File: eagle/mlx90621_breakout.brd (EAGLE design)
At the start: 53.3 x 59.7 mm, 16 parts, among them J1 ARDUINO_R3_SHIELD

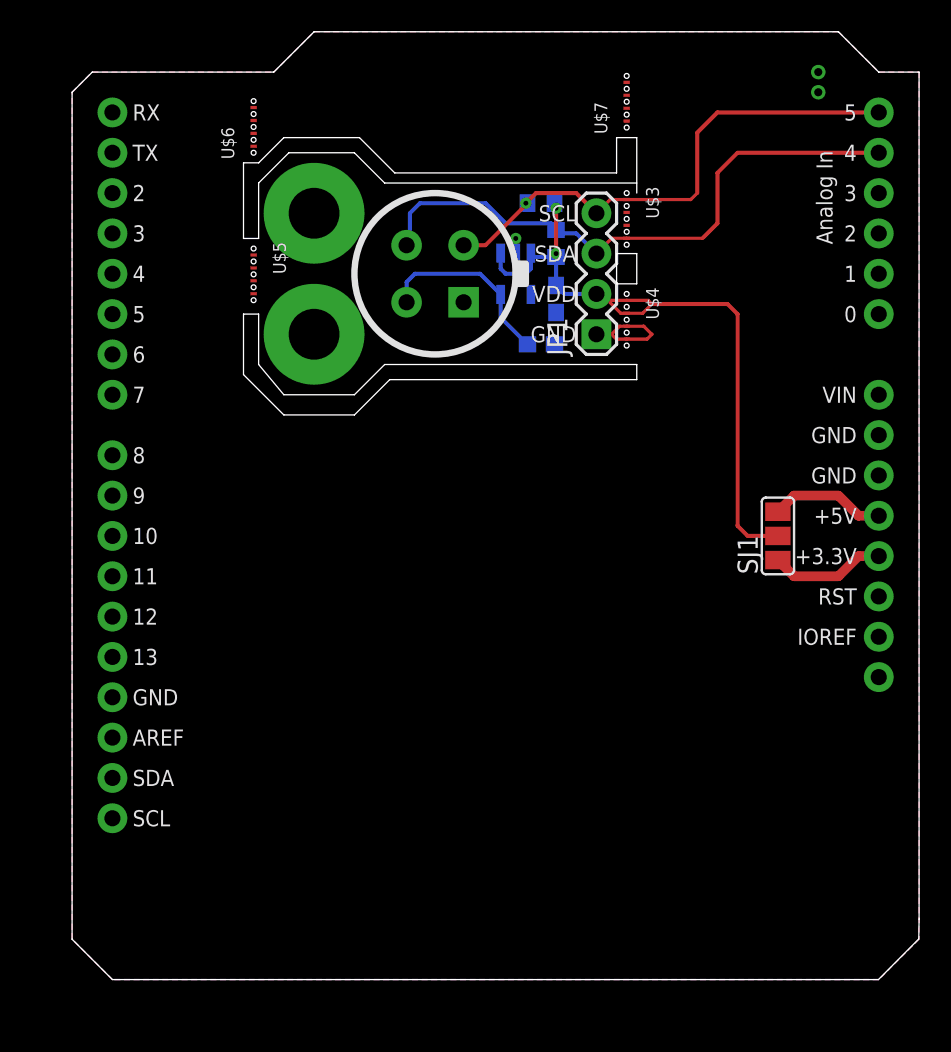
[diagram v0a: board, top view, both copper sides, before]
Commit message: cleaned breakout for better component counting at BOM generation
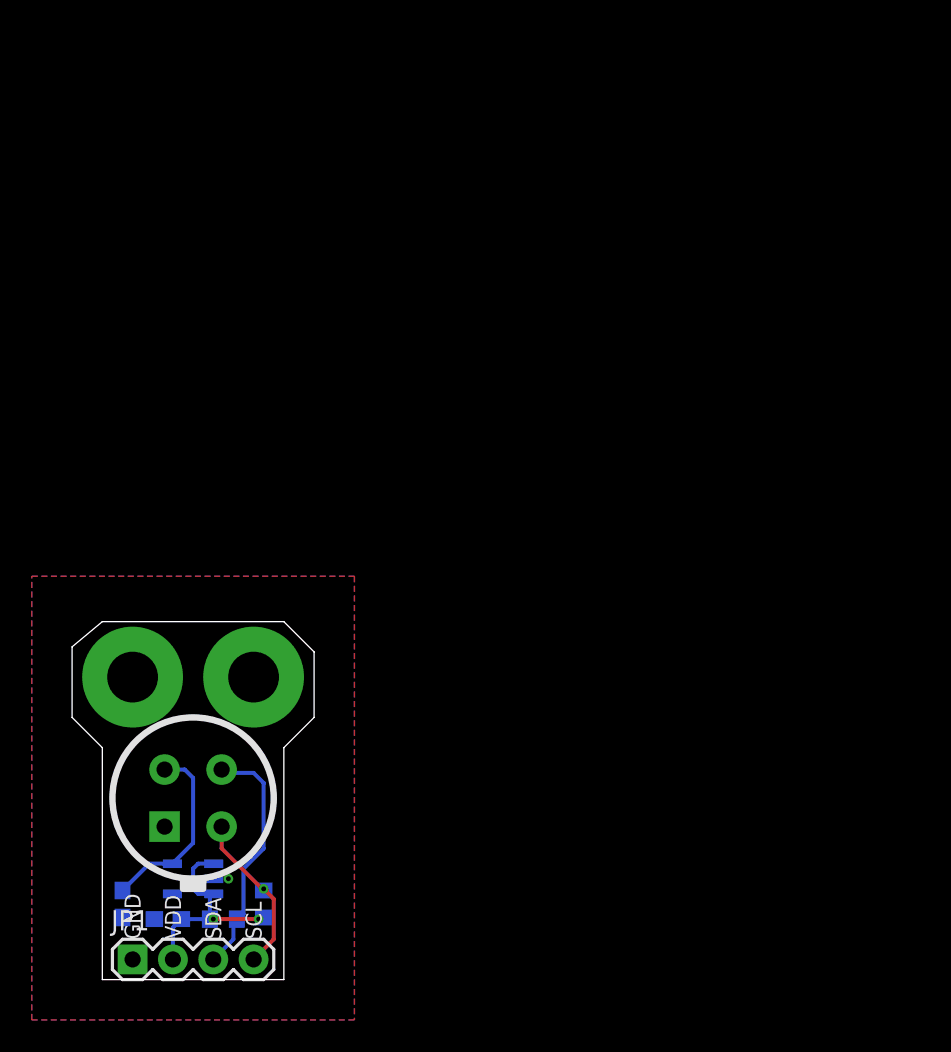
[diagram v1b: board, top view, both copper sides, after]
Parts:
- removed J1: ARDUINO_R3_SHIELD, SparkFun-Boards:UNO_R3_SHIELD
- removed SJ1: (no value), jumper:SJ_2
- removed U$3, U$4, U$5, U$6, U$7: MOUSE-BITES-4, mouse-bites:MOUSE-BITES-4
- moved JP1 49.0 mm to (3.81, 1.27), turned to 0 degrees
- moved R1 47.5 mm to (12.1, 4.76), turned to 270 degrees
- moved R2 47.4 mm to (9.53, 3.81), turned to 0 degrees
- moved C1 46.1 mm to (6.03, 3.81), turned to 0 degrees
- moved C2 44.0 mm to (3.17, 4.76), turned to 270 degrees
- moved U$2 43.2 mm to (7.62, 6.35), turned to 270 degrees
- moved U$1 36.4 mm to (7.62, 11.4), turned to 0 degrees
- moved S2 29.5 mm to (11.4, 19.1), turned to 0 degrees
- moved S1 24.4 mm to (3.81, 19.1), turned to 0 degrees
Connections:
- removed net +3V3: J1.3.3V, SJ1.1
- removed net +5V: J1.5V, SJ1.3
- net GND: no longer J1.GND@0, J1.GND@1, J1.GND@2, U$4.3, U$4.4
- net SCL: no longer J1.A5, U$3.1
- net SDA: no longer J1.A4, U$3.4
- net VCC: no longer SJ1.2, U$4.1, U$4.2
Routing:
- net VCC: track 42.7 -> 13.8 mm
- net SCL: track 33.9 -> 11.3 mm
- net SDA: track 37.8 -> 15.5 mm
- net +3V3: track 7.30 -> 0.00 mm
- net +5V: track 7.30 -> 0.00 mm
- net GND: track 7.02 -> 0.00 mm, vias 3 -> 1
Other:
- board size 53.3 x 59.7 mm -> 15.2 x 22.5 mm

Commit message: changed References for ICs (U1, U2)
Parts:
- renumbered U$1 to U1, U$2 to U2
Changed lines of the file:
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@@
 <attribute name="VALUE" x="8.636" y="3.175" size="0.8128" layer="28" font="vector" rot="MR180"/>
 </element>
-<element name="U$1" library="melexis" package="MLX90621" value="MLX90621BAD" x="7.62" y="11.43" smashed="yes" rot="MR0">
+<element name="U1" library="melexis" package="MLX90621" value="MLX90621BAD" x="7.62" y="11.43" smashed="yes" rot="MR0">
 <attribute name="NAME" x="12.7" y="3.81" size="1.27" layer="26" rot="MR0"/>
 <attribute name="VALUE" x="11.176" y="10.922" size="0.8128" layer="28" rot="MR0"/>
 </element>
-<element name="U$2" library="melexis" package="VREG_SOT23-5" value="ZXCL260" x="7.62" y="6.35" smashed="yes" rot="MR270">
+<element name="U2" library="melexis" package="VREG_SOT23-5" value="ZXCL260" x="7.62" y="6.35" smashed="yes" rot="MR270">
 <attribute name="NAME" x="5.461" y="7.239" size="0.4064" layer="26" rot="MR270"/>
 <attribute name="VALUE" x="7.1755" y="5.2705" size="0.8128" layer="28" font="vector" rot="MR90"/>
@@
 <signals>
 <signal name="VDD">
-<contactref element="U$1" pad="VDD"/>
-<contactref element="U$2" pad="5"/>
+<contactref element="U1" pad="VDD"/>
+<contactref element="U2" pad="5"/>
 <contactref element="C2" pad="1"/>
 <wire x1="3.175" y1="5.6125" x2="4.8625" y2="7.3" width="0.254" layer="16"/>
@@
 </signal>
 <signal name="GND">
-<contactref element="U$2" pad="2"/>
+<contactref element="U2" pad="2"/>
 <contactref element="C1" pad="2"/>
 <contactref element="C2" pad="2"/>
-<contactref element="U$1" pad="VSS"/>
+<contactref element="U1" pad="VSS"/>
 <polygon width="0.508" layer="1">
 <vertex x="-2.54" y="-2.54"/>
@@
 </signal>
 <signal name="VCC">
-<contactref element="U$2" pad="1"/>
+<contactref element="U2" pad="1"/>
 <contactref element="C1" pad="1"/>
 <contactref element="R1" pad="2"/>
 <contactref element="R2" pad="2"/>
-<contactref element="U$2" pad="3"/>
+<contactref element="U2" pad="3"/>
 <contactref element="JP1" pad="2"/>
 <wire x1="6.35" y1="1.27" x2="6.35" y2="3.2775" width="0.254" layer="16"/>
@@
 </signal>
 <signal name="SDA">
-<contactref element="U$1" pad="SDA"/>
+<contactref element="U1" pad="SDA"/>
 <contactref element="R2" pad="1"/>
 <contactref element="JP1" pad="3"/>
@@
 </signal>
 <signal name="SCL">
-<contactref element="U$1" pad="SCL"/>
+<contactref element="U1" pad="SCL"/>
 <contactref element="R1" pad="1"/>
 <contactref element="JP1" pad="4"/>
